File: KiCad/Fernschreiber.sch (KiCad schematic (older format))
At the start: 38 parts, among them J1 Step-Up, J10 Conn_01x01_Male, J11 Conn_01x01_Male, J2 Fernschreiber, J3 Conn_01x02_Male, J4 Conn_01x02_Male, J5 TX,RX,3V3,GND, J6 Conn_01x01_Male, J7 12,13,14,3V3,GND, J8 18,19,23,3V3,GND, J9 Conn_01x01_Male, K1 FINDER-40.41, K2 FINDER-40.41, Q1 Q_NMOS_SGD, Q2 Q_NMOS_SGD, U1 4N28, U2 ESP32-WROOM-32, U3 4N28

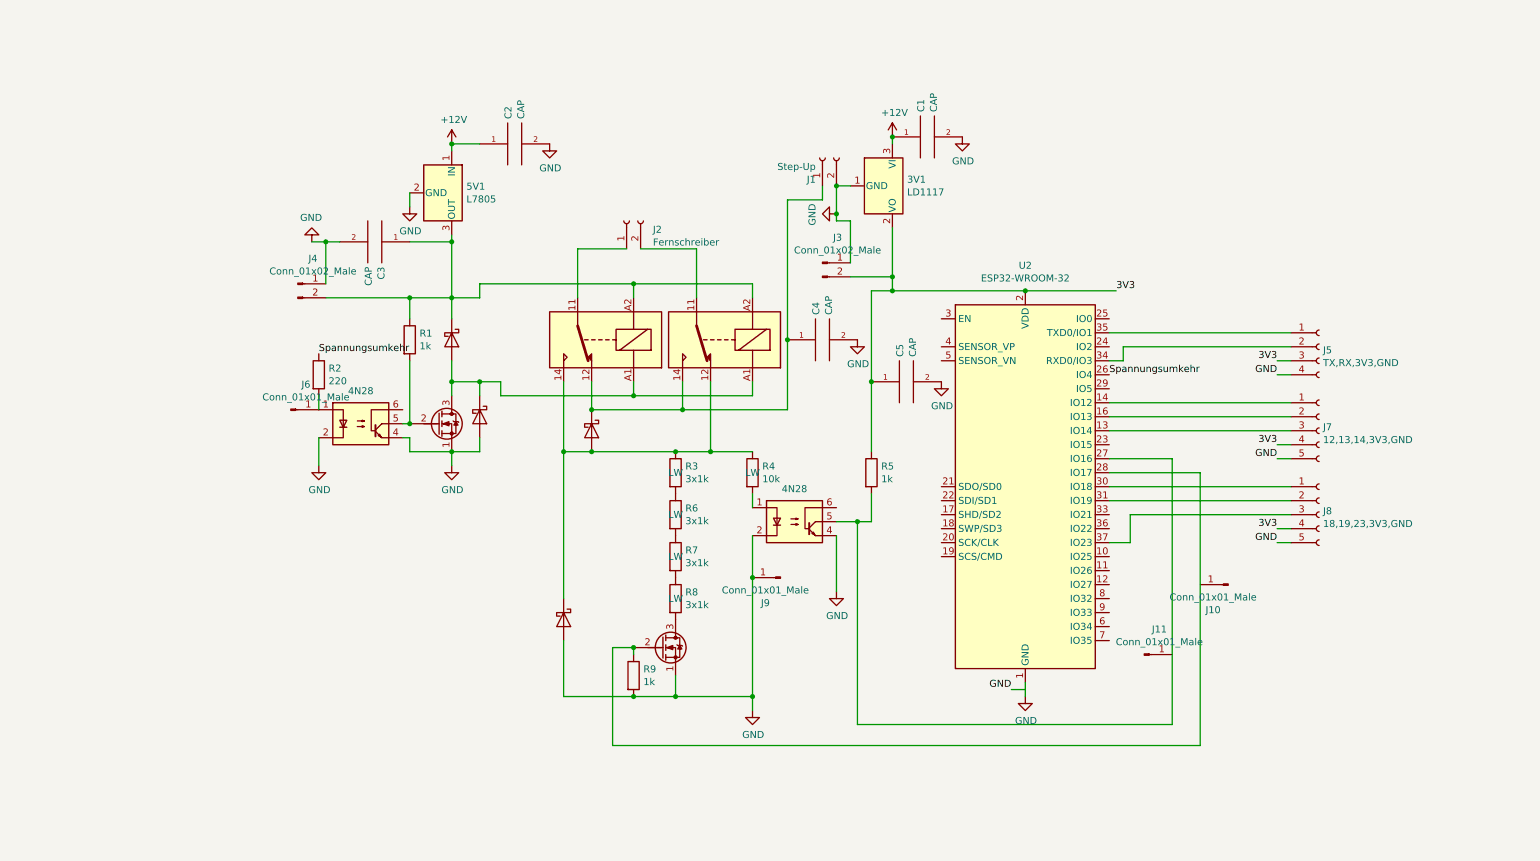
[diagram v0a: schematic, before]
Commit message: Modified Footprints, routing PCB(not finished yet)
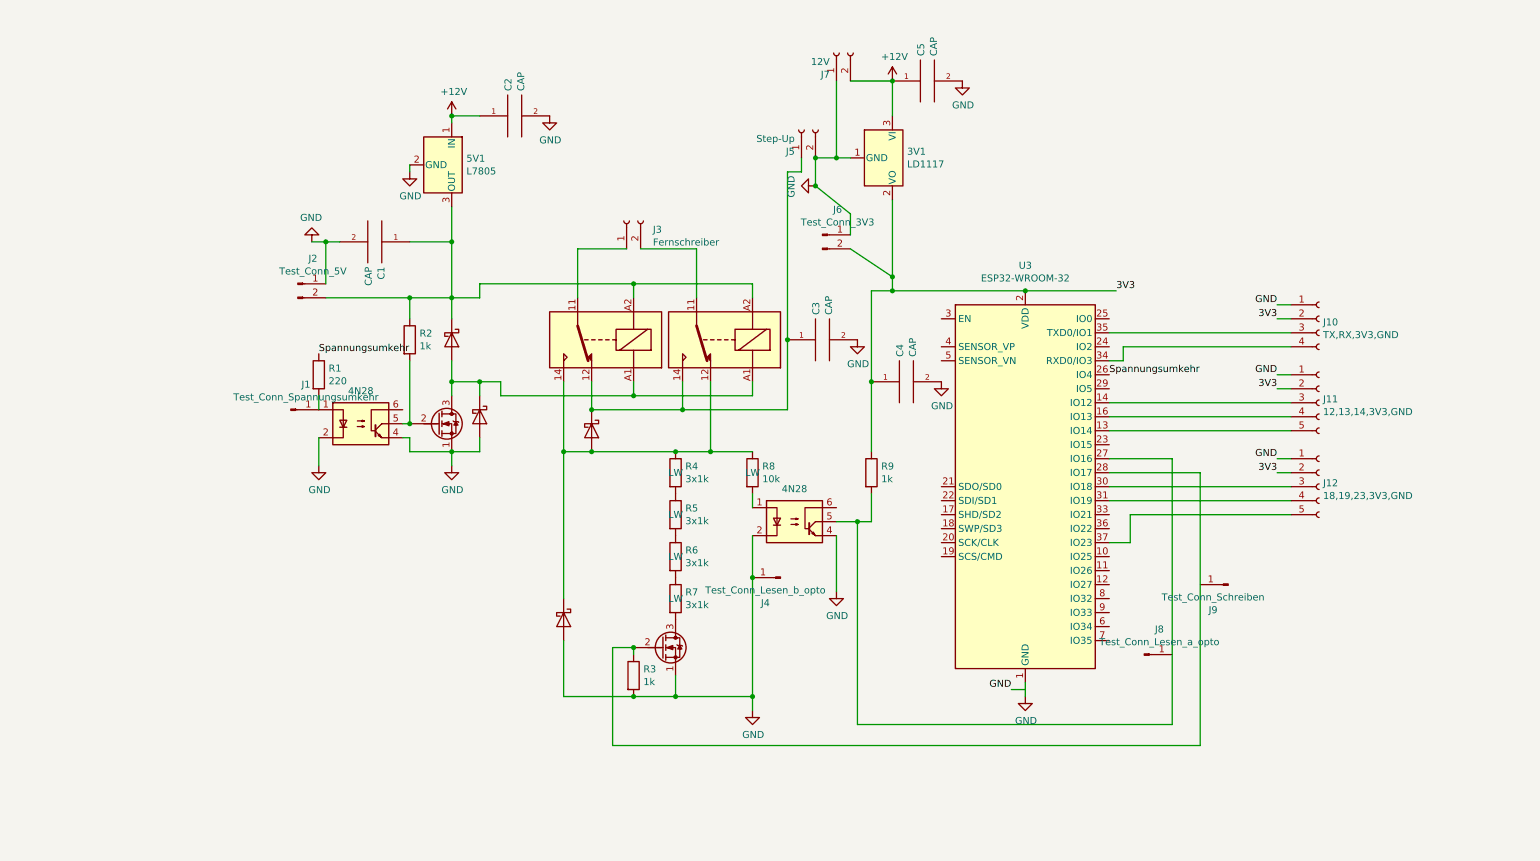
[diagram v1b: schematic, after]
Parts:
- added J7: 12V, Fernschreiber:DECA MB310-500M02 Schraubklemmblock, symbol Connector:Conn_01x02_Female
- J1: renamed from J6; value Conn_01x01_Male -> Test_Conn_Spannungsumkehr; footprint (none) -> Connector_PinHeader_2.54mm:PinHeader_1x01_P2.54mm_Vertical
- J2: renamed from J4; value Conn_01x02_Male -> Test_Conn_5V; footprint (none) -> Connector_PinHeader_2.54mm:PinHeader_1x02_P2.54mm_Vertical
- J4: renamed from J9; value Conn_01x01_Male -> Test_Conn_Lesen_b_opto; footprint (none) -> Connector_PinHeader_2.54mm:PinHeader_1x01_P2.54mm_Vertical
- J6: renamed from J3; value Conn_01x02_Male -> Test_Conn_3V3; footprint (none) -> Connector_PinHeader_2.54mm:PinHeader_1x02_P2.54mm_Vertical
- J8: renamed from J11; value Conn_01x01_Male -> Test_Conn_Lesen_a_opto; footprint (none) -> Connector_PinHeader_2.54mm:PinHeader_1x01_P2.54mm_Vertical
- J9: renamed from J10; value Conn_01x01_Male -> Test_Conn_Schreiben; footprint (none) -> Connector_PinHeader_2.54mm:PinHeader_1x01_P2.54mm_Vertical
- renumbered C3 to C1, C4 to C3, C5 to C4, C1 to C5, D4 to D3, D3 to D4, J5 to J10, J7 to J11, J8 to J12, J2 to J3, J1 to J5, R2 to R1, R1 to R2, R9 to R3, R3 to R4, R6 to R5, R7 to R6, R8 to R7, R4 to R8, R5 to R9, U3 to U2, U2 to U3
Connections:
- net +12V: now also J7.2 (Pin_2)
- net 3V3: now also J10.2 (Pin_2), J11.2 (Pin_2), J12.2 (Pin_2); no longer J10.3 (Pin_3), J11.4 (Pin_4), J12.4 (Pin_4)
- net GND: now also J10.1 (Pin_1), J11.1 (Pin_1), J12.1 (Pin_1), J7.1 (Pin_1); no longer J10.4 (Pin_4), J11.5 (Pin_5), J12.5 (Pin_5)
- net at U3.13 (IO14): now also J11.5 (Pin_5); no longer J11.3 (Pin_3)
- net at U3.14 (IO12): now also J11.3 (Pin_3); no longer J11.1 (Pin_1)
- net at U3.16 (IO13): now also J11.4 (Pin_4); no longer J11.2 (Pin_2)
- net at U3.30 (IO18): now also J12.3 (Pin_3); no longer J12.1 (Pin_1)
- net at U3.31 (IO19): now also J12.4 (Pin_4); no longer J12.2 (Pin_2)
- net at U3.34 (RXD0/IO3): now also J10.4 (Pin_4); no longer J10.2 (Pin_2)
- net at U3.35 (TXD0/IO1): now also J10.3 (Pin_3); no longer J10.1 (Pin_1)
- net at U3.37 (IO23): now also J12.5 (Pin_5); no longer J12.3 (Pin_3)
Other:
- moved on the sheet: 3V1, 5V1, C2, C5, J10, J11, J12, J5, J6

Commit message: Finished routing PCB + updated Footprints + updated Symbols + updated Schematic + ordered PCB at JLCPCB
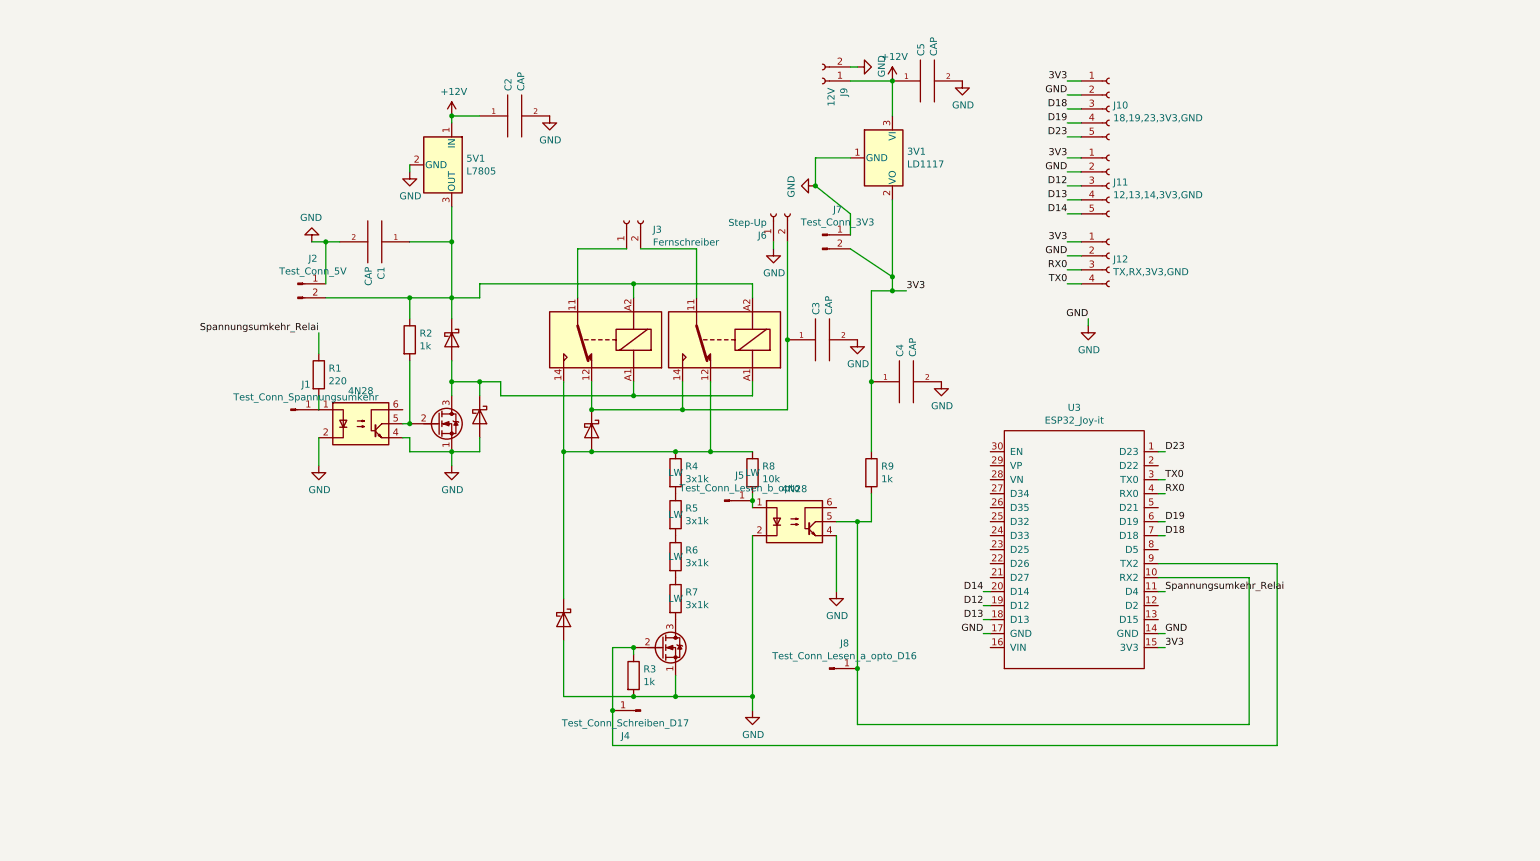
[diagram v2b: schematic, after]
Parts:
- removed U3: ESP32-WROOM-32, Fernschreiber:ESP32_Joy-it, symbol RF_Module:ESP32-WROOM-32
- added U3: ESP32_Joy-it, Fernschreiber:ESP32_Joy-it, symbol Fernschreiber:ESP32_Joy-it
- J4: renamed from J9; value Test_Conn_Schreiben -> Test_Conn_Schreiben_D17
- J8: value Test_Conn_Lesen_a_opto -> Test_Conn_Lesen_a_opto_D16
- renumbered J12 to J10, J10 to J12, J4 to J5, J5 to J6, J6 to J7, J7 to J9
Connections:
- net +12V: now also J9.1 (Pin_1); no longer J9.2 (Pin_2)
- net 3V3: now also J10.1 (Pin_1), J11.1 (Pin_1), J12.1 (Pin_1), U3.15 (3V3); no longer J10.2 (Pin_2), J11.2 (Pin_2), J12.2 (Pin_2)
- net GND: now also J10.2 (Pin_2), J11.2 (Pin_2), J12.2 (Pin_2), J6.1 (Pin_1), J9.2 (Pin_2), U3.14 (GND), U3.17 (GND); no longer J10.1 (Pin_1), J11.1 (Pin_1), J12.1 (Pin_1), J5.1 (Pin_1), J6.2 (Pin_2), J9.1 (Pin_1)
- net at R8.2, U2.1: now also J5.1 (Pin_1)
- net at R9.2, U2.5: now also J8.1 (Pin_1), U3.10 (RX2)
- net at Q2.2 (G), R3.1: now also J4.1 (Pin_1), U3.9 (TX2)
- net at C3.1, D4.1 (K), K1.12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: now also J6.2 (Pin_2); no longer J6.1 (Pin_1)
- net D14: now reaches J11.5 (Pin_5)
- net D14: now also U3.20 (D14)
- net D12: now reaches J11.3 (Pin_3)
- net D12: now also U3.19 (D12)
- net D13: now reaches J11.4 (Pin_4)
- net D13: now also U3.18 (D13)
- net D18: now reaches J10.3 (Pin_3)
- net D18: now also U3.7 (D18)
- net D19: now reaches J10.4 (Pin_4)
- net D19: now also U3.6 (D19)
- net TX0: now reaches J12.4 (Pin_4)
- net TX0: now also U3.3 (TX0)
- net RX0: now reaches J12.3 (Pin_3)
- net RX0: now also U3.4 (RX0)
- net D23: now reaches J10.5 (Pin_5)
- net D23: now also U3.1 (D23)
- net Spannungsumkehr renamed Spannungsumkehr_Relai
- net Spannungsumkehr_Relai: now also U3.11 (D4)
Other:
- moved on the sheet: J10, J11, J12, J4, J5, J6, J8, J9

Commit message: Changed schemetic removed powersupply changed opto read connection removed Diode 4 overall improved schemetic
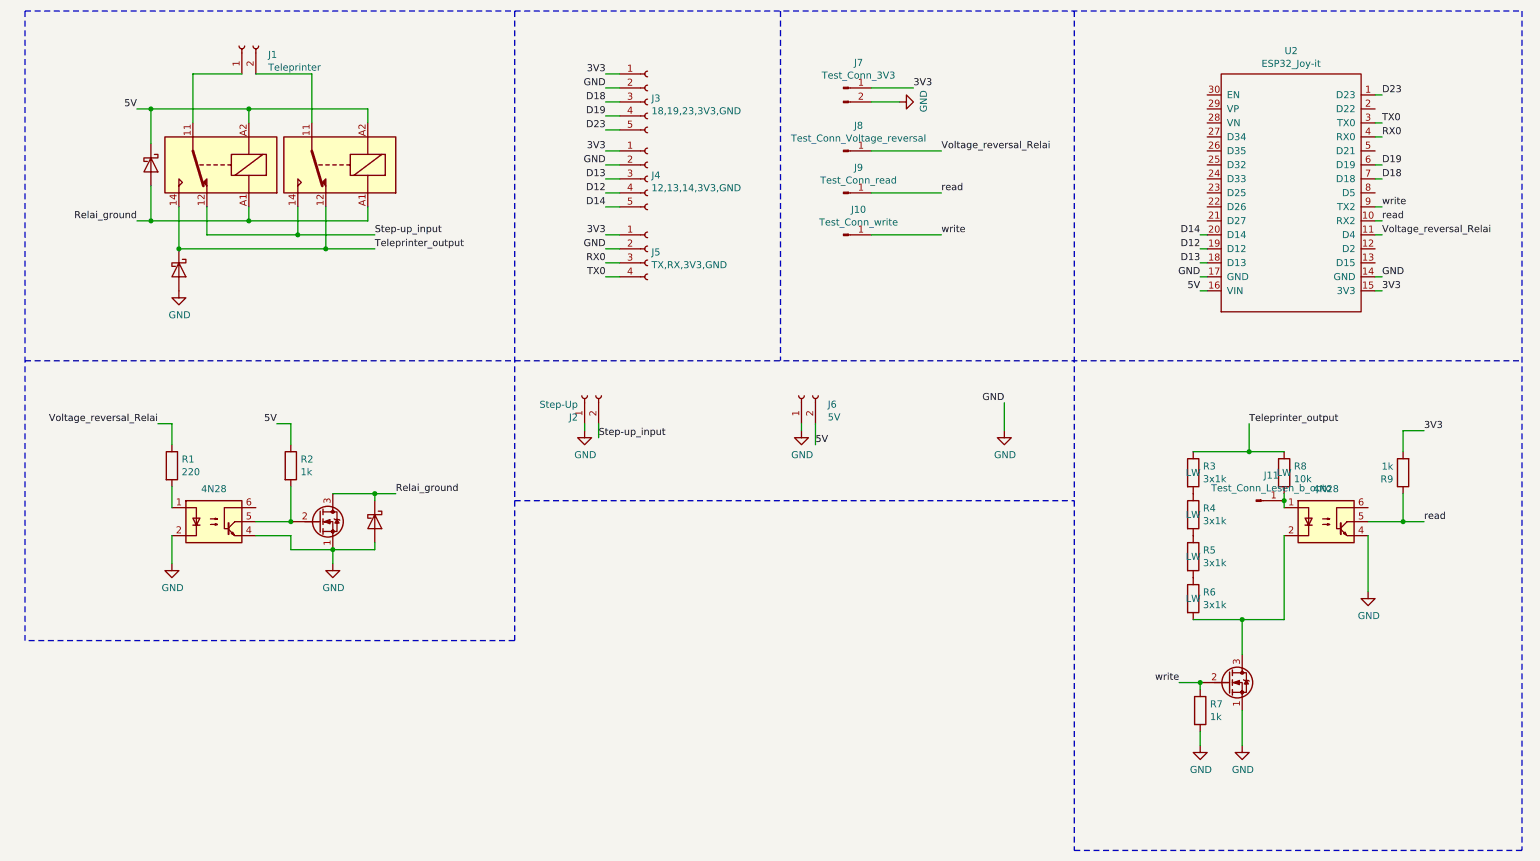
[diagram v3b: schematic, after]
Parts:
- removed 3V1: LD1117, Fernschreiber:LD1117, symbol Regulator_Linear:LD1117S12TR_SOT223
- removed 5V1: L7805, Fernschreiber:L7805AB, symbol Regulator_Linear:L7805
- removed C1, C2, C3, C4, C5: CAP, Capacitor_THT:CP_Radial_D7.5mm_P2.50mm, symbol pspice:CAP
- removed D4: 1N5711, Diode_THT:D_DO-35_SOD27_P7.62mm_Horizontal, symbol Diode:1N5711
- removed J2: Test_Conn_5V, Connector_PinHeader_2.54mm:PinHeader_1x02_P2.54mm_Vertical, symbol Connector:Conn_01x02_Male
- removed J9: 12V, Fernschreiber:DECA MB310-500M02 Schraubklemmblock, symbol Connector:Conn_01x02_Female
- added J6: 5V, Fernschreiber:DECA MB310-500M02 Schraubklemmblock, symbol Connector:Conn_01x02_Female
- D1: footprint Diode_THT:D_DO-35_SOD27_P7.62mm_Horizontal -> Diode_THT:D_DO-201AE_P15.24mm_Horizontal
- D2: renamed from D3; footprint Diode_THT:D_DO-35_SOD27_P7.62mm_Horizontal -> Diode_THT:D_DO-201AE_P15.24mm_Horizontal
- D3: renamed from D2; footprint Diode_THT:D_DO-35_SOD27_P7.62mm_Horizontal -> Diode_THT:D_DO-201AE_P15.24mm_Horizontal
- J1: renamed from J3; value Fernschreiber -> Teleprinter
- J10: renamed from J4; value Test_Conn_Schreiben_D17 -> Test_Conn_write
- J8: renamed from J1; value Test_Conn_Spannungsumkehr -> Test_Conn_Voltage_reversal
- J9: renamed from J8; value Test_Conn_Lesen_a_opto_D16 -> Test_Conn_read
- R1, R2, R9: footprint Resistor_THT:R_Axial_DIN0414_L11.9mm_D4.5mm_P20.32mm_Horizontal -> Resistor_THT:R_Axial_DIN0411_L9.9mm_D3.6mm_P12.70mm_Horizontal
- R7: renamed from R3; footprint Resistor_THT:R_Axial_DIN0414_L11.9mm_D4.5mm_P20.32mm_Horizontal -> Resistor_THT:R_Axial_DIN0411_L9.9mm_D3.6mm_P12.70mm_Horizontal
- R8: footprint Resistor_THT:R_Axial_DIN0414_L11.9mm_D4.5mm_P25.40mm_Horizontal -> Resistor_THT:R_Axial_DIN0414_L11.9mm_D4.5mm_P15.24mm_Horizontal
- renumbered J5 to J11, J6 to J2, J10 to J3, J11 to J4, J12 to J5, R4 to R3, R5 to R4, R6 to R5, R7 to R6, U3 to U2, U2 to U3
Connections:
- net 3V3: now also J7.1 (Pin_1), R9.2; no longer J7.2 (Pin_2), R9.1
- net D12: now also J4.4 (Pin_4); no longer J4.3 (Pin_3)
- net D13: now also J4.3 (Pin_3); no longer J4.4 (Pin_4)
- net GND: now also J7.2 (Pin_2), J6.1 (Pin_1); no longer J7.1 (Pin_1), U3.2
- net read: now reaches J9.1 (Pin_1), U2.10 (RX2), U3.5
- net read: now also R9.1; no longer R9.2
- net Teleprinter_output: now reaches D2.1 (K), K1.14, K2.12, R3.1, R8.1
- net write: now reaches J10.1 (Pin_1), Q2.2 (G), R7.1, U2.9 (TX2)
- net at Q2.3 (D), R6.2: now also U3.2
- net Step-up_input: now reaches J2.2 (Pin_2), K1.12, K2.14
- net Relai_ground: now reaches D1.2 (A), D3.1 (K), K1.A1, K2.A1, Q1.3 (D)
- net 5V: now reaches D1.1 (K), K1.A2, K2.A2, R2.1
- net 5V: now also U2.16 (VIN), J6.2 (Pin_2)
- net at R1.2, U1.1: no longer J8.1 (Pin_1)
- net Spannungsumkehr_Relai renamed Voltage_reversal_Relai
- net Voltage_reversal_Relai: now also J8.1 (Pin_1)
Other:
- moved on the sheet: J1, J10, J11, J2, J3, J4, J5, J7, J8, J9, R1, R2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
